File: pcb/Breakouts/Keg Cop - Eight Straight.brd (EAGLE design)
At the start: 49 x 69 mm, 12 parts

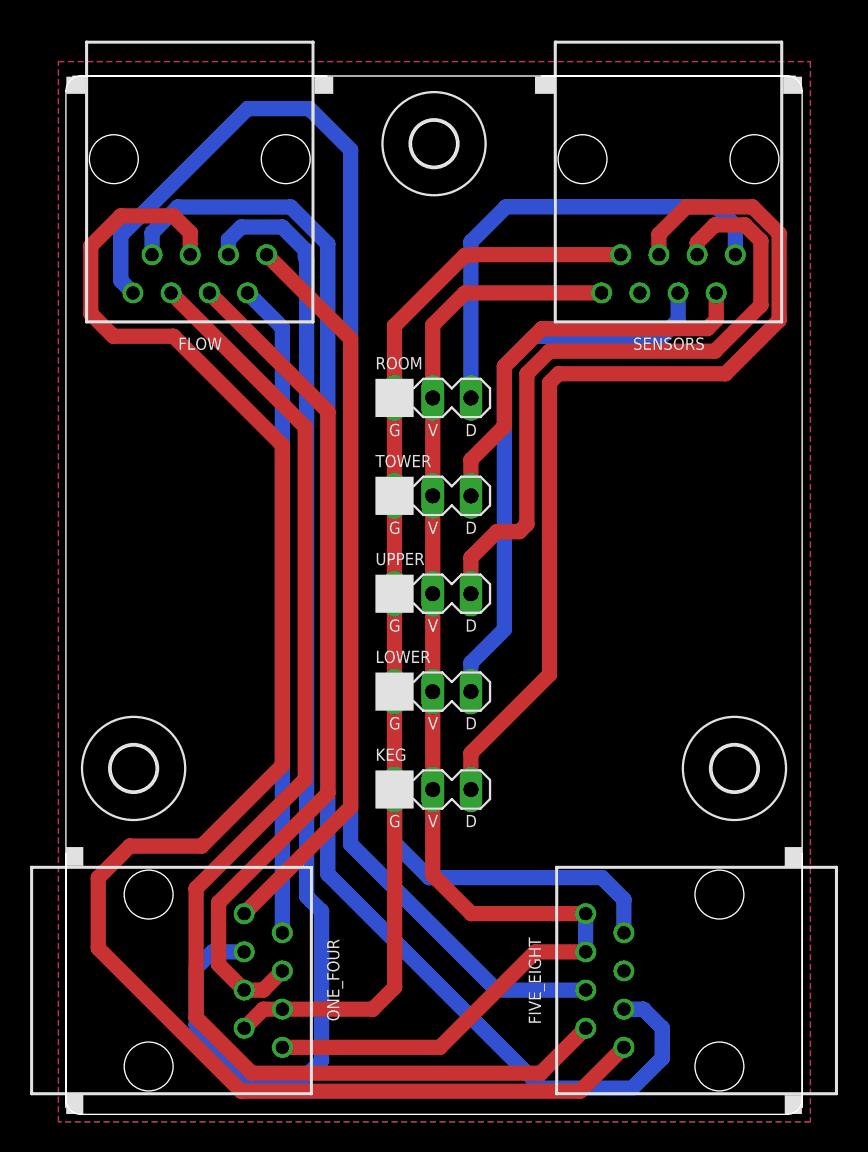
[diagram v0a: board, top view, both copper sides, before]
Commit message: Re-work pour
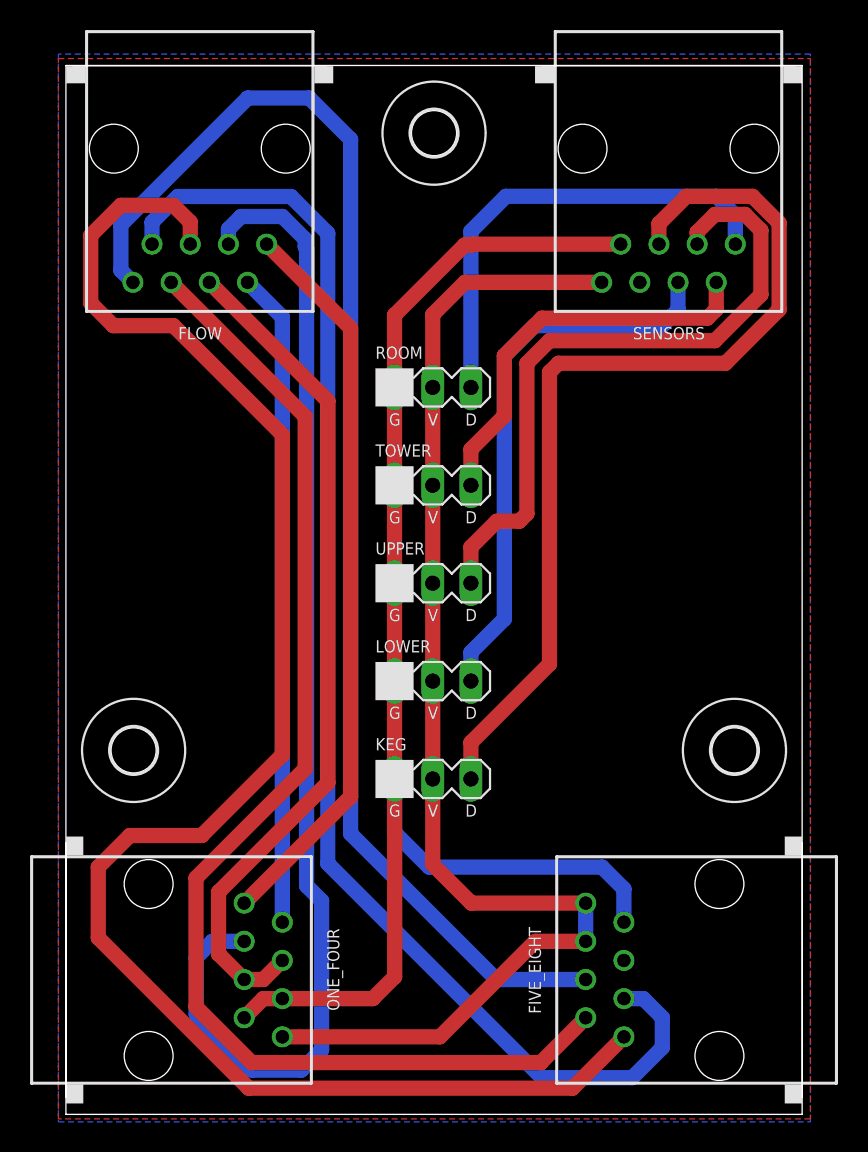
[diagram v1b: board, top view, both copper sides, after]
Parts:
- moved U$1 1.20 mm to (4.50, 24.2)
- moved U$2 1.20 mm to (44.5, 24.2)
- moved ROOM 0.70 mm to (21.8, 48.3)
- moved TOWER 0.70 mm to (21.8, 41.8)
- moved UPPER 0.70 mm to (21.8, 35.3)
- moved FIVE_EIGHT 0.70 mm to (43.5, 9.60)
- moved KEG 0.70 mm to (21.8, 22.3)
- moved LOWER 0.70 mm to (21.8, 28.8)
- moved ONE_FOUR 0.70 mm to (5.50, 9.60)
- moved FLOW 0.70 mm to (8.90, 64.2)
- moved SENSORS 0.70 mm to (40.1, 64.2)
- moved U$3 0.70 mm to (24.5, 65.2)
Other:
- board size 49 x 69 mm -> 49 x 69.7 mm
